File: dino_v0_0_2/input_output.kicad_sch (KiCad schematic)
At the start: 26 parts, among them SW1 SW_DIP_x08

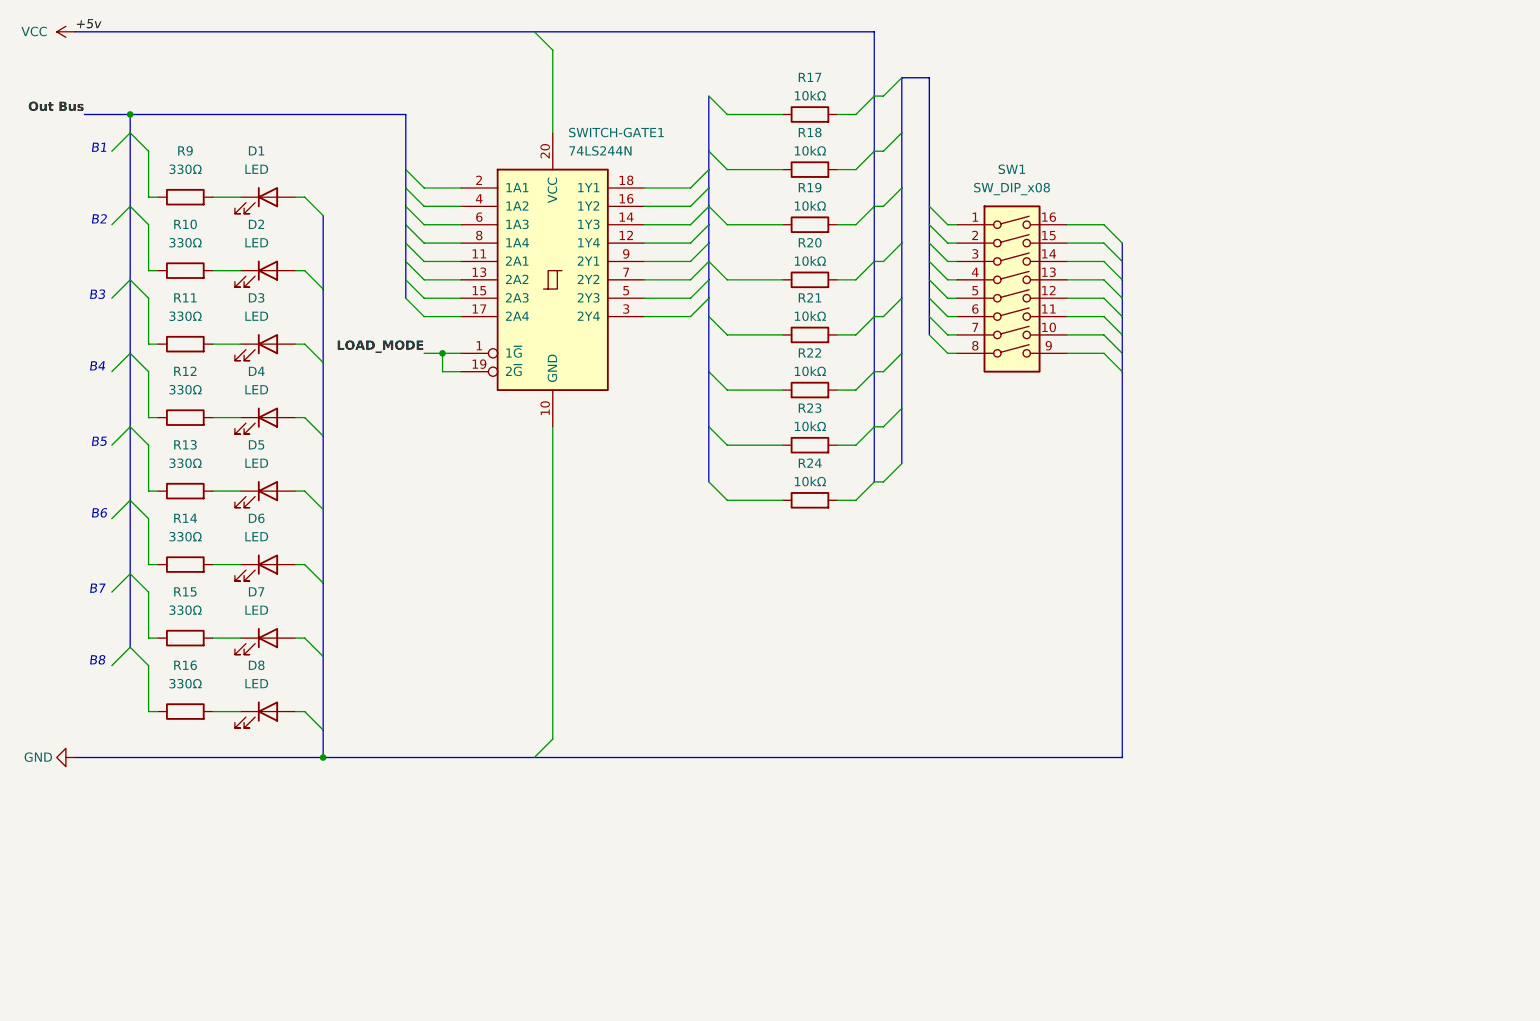
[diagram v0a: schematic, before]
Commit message: DINO v0.0.3: complete ALU/control-word, add MAR+reset sheets, wire reset circuit
ALU sheet: flags register moved from '173 (not in stock) to '273 + a '157
mux to emulate the missing load-enable pins; Z-detect built from a NOR+AND
De Morgan tree instead of a '260; ALU_CIN built from NAND(SA1,SA0) reusing
two already-placed spare gates instead of a dedicated XOR/'86. Sheet is
now fully wired and netlist-clean.

Control word sheet: all 16 CW bits assigned and wired (3x '138 decoders
for the load/source/misc fields, direct bus taps for HALT/PC_MAR_MUX/
PC_UP/END and the ALU SA[2:0] select). Found and fixed several cross-
sheet signal-name mismatches this uncovered (OUT_REG_LOAD/REG_OUT_LOAD,
PC_MAR_MUX/PC_MUX, T-state counter labels, a mirror-reversed IRB->ROM-
address buffer in microcode).

New: MAR and reset sheets, wired into the root hierarchy. Reset circuit
is a from-scratch design: RC+button+74HC14 Schmitt front end feeds the
async PRESET of the clock cluster's spare '74 half (U27B), synchronizing
release to CLK; its Q/~Q fan out to the flags register, the T-state
counter's clear, and (OR'd with the existing microcode-driven PC_CLEAR,
reusing spare gates on the same '02) the PC counters' clear.

Deprecated 7 schematic files no longer referenced by the root sheet's
hierarchy into dino_v0_0_2/deprecated/. Added docs/notes/kicad_netlist.py,
a .kicad_sch connectivity auditor (pin/net resolution incl. buses and
same-name local-label merging) used throughout this session to find the
above bugs; archived completed-work docs into docs/notes/Done/ and
rewrote dino_session_state.md as the current authoritative state+TODO.

Co-Authored-By: Claude Sonnet 5 <noreply@anthropic.com>
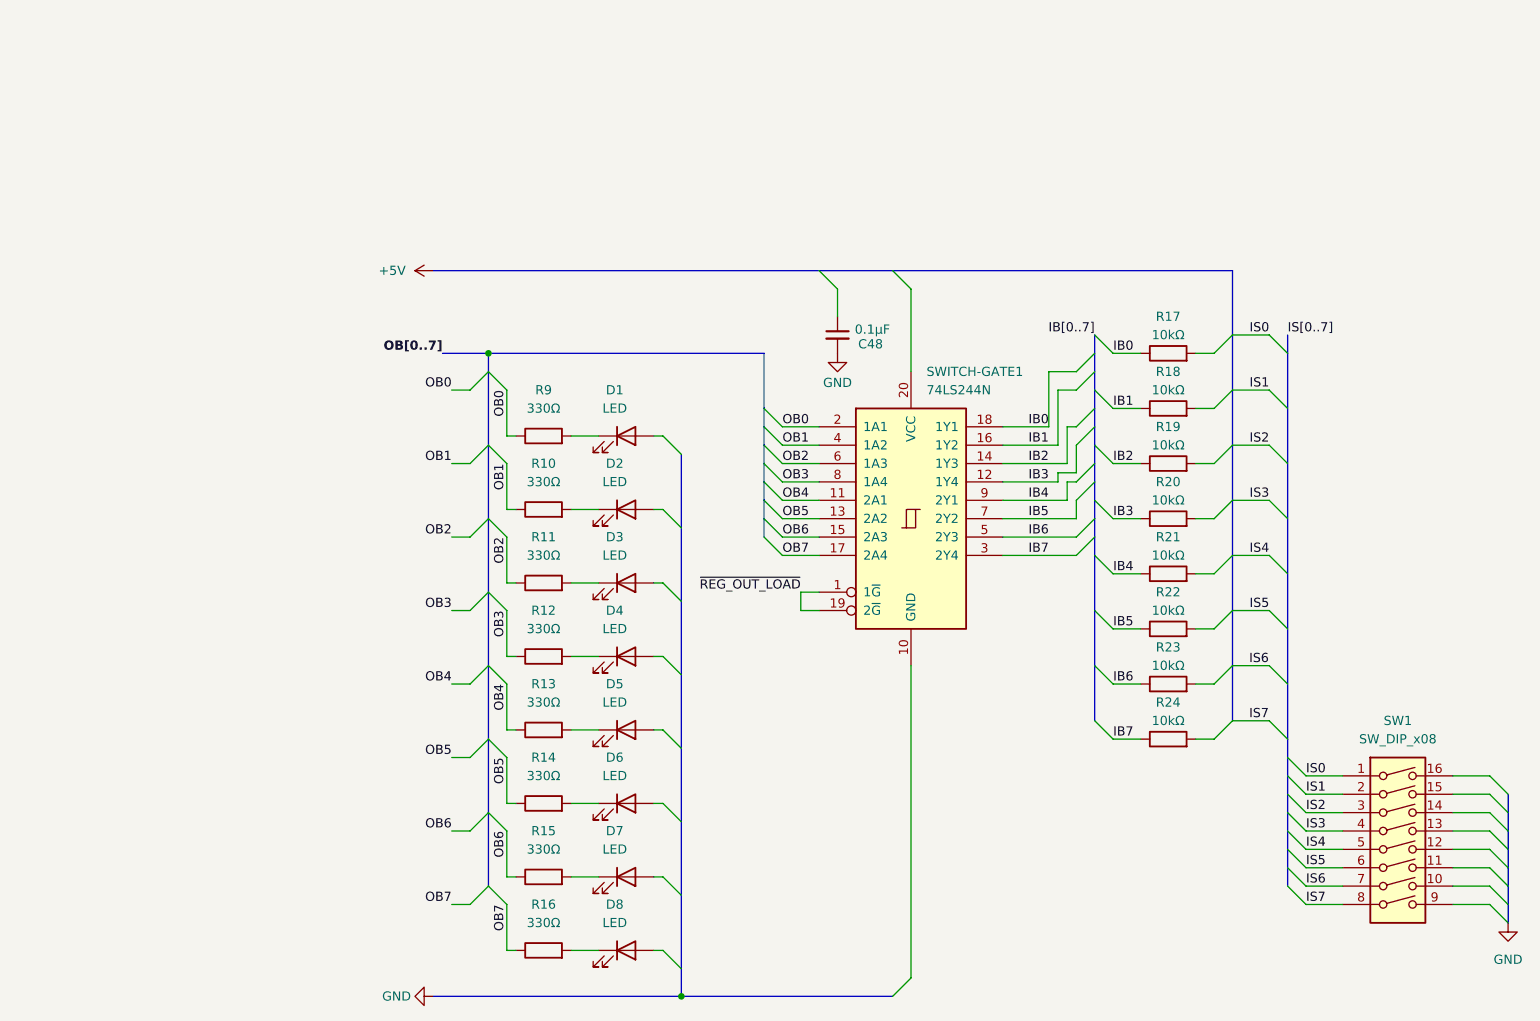
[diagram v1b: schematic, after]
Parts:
- added C48: 0.1µF, symbol Device:C_Small
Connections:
- net GND: now also C48.2
- net OB1: now reaches R10.1
- net OB1: now also SWITCH-GATE1.4 (1A2)
- net IB6: now reaches R23.1
- net IB6: now also SWITCH-GATE1.5 (2Y3)
- net IB2: now reaches R19.1
- net IB2: now also SWITCH-GATE1.14 (1Y3)
- net OB5: now reaches R14.1
- net OB5: now also SWITCH-GATE1.13 (2A2)
- net IB4: now reaches R21.1
- net IB4: now also SWITCH-GATE1.9 (2Y1)
- net OB4: now reaches R13.1
- net OB4: now also SWITCH-GATE1.11 (2A1)
- net OB0: now reaches R9.1
- net OB0: now also SWITCH-GATE1.2 (1A1)
- net IB7: now reaches R24.1
- net IB7: now also SWITCH-GATE1.3 (2Y4)
- net IB3: now reaches R20.1
- net IB3: now also SWITCH-GATE1.12 (1Y4)
- net OB6: now reaches R15.1
- net OB6: now also SWITCH-GATE1.15 (2A3)
- net IB1: now reaches R18.1
- net IB1: now also SWITCH-GATE1.16 (1Y2)
- net OB7: now reaches R16.1
- net OB7: now also SWITCH-GATE1.17 (2A4)
- net OB3: now reaches R12.1
- net OB3: now also SWITCH-GATE1.8 (1A4)
- net OB2: now reaches R11.1
- net OB2: now also SWITCH-GATE1.6 (1A3)
- net IB5: now reaches R22.1
- net IB5: now also SWITCH-GATE1.7 (2Y2)
- net IS0: now reaches SW1.1
- net IS1: now reaches SW1.2
- net IS2: now reaches SW1.3
- net IS3: now reaches SW1.4
- net IS4: now reaches SW1.5
- net IS5: now reaches SW1.6
- net IS6: now reaches SW1.7
- net IS7: now reaches SW1.8
- net IB0: now reaches R17.1
- net IB0: now also SWITCH-GATE1.18 (1Y1)
- net LOAD_MODE renamed ~{REG_OUT_LOAD}
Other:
- note removed: "B1"
- note removed: "B2"
- note removed: "B3"
- note removed: "B4"
- note removed: "B5"
- note removed: "B6"
- note removed: "B7"
- note removed: "B8"
- moved on the sheet: D1, D2, D3, D4, D5, D6, D7, D8, R10, R11, R12, R13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
